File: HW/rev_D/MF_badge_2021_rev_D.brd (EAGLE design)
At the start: 61 x 100.5 mm, 167 parts, among them IC1 MCP73831, J1 HRO_31_M_12_USB_C, Q2 DMG3415U-7, Q3 DMG3415U-7, Q4 DMG3415U-7, Q5 Si2305, Q6 SI1308EDL-T1-GE3, U1 ESP32-S2-WROOM, U2 AP2112K-3.3, X1 CAPTOUCH_10MM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

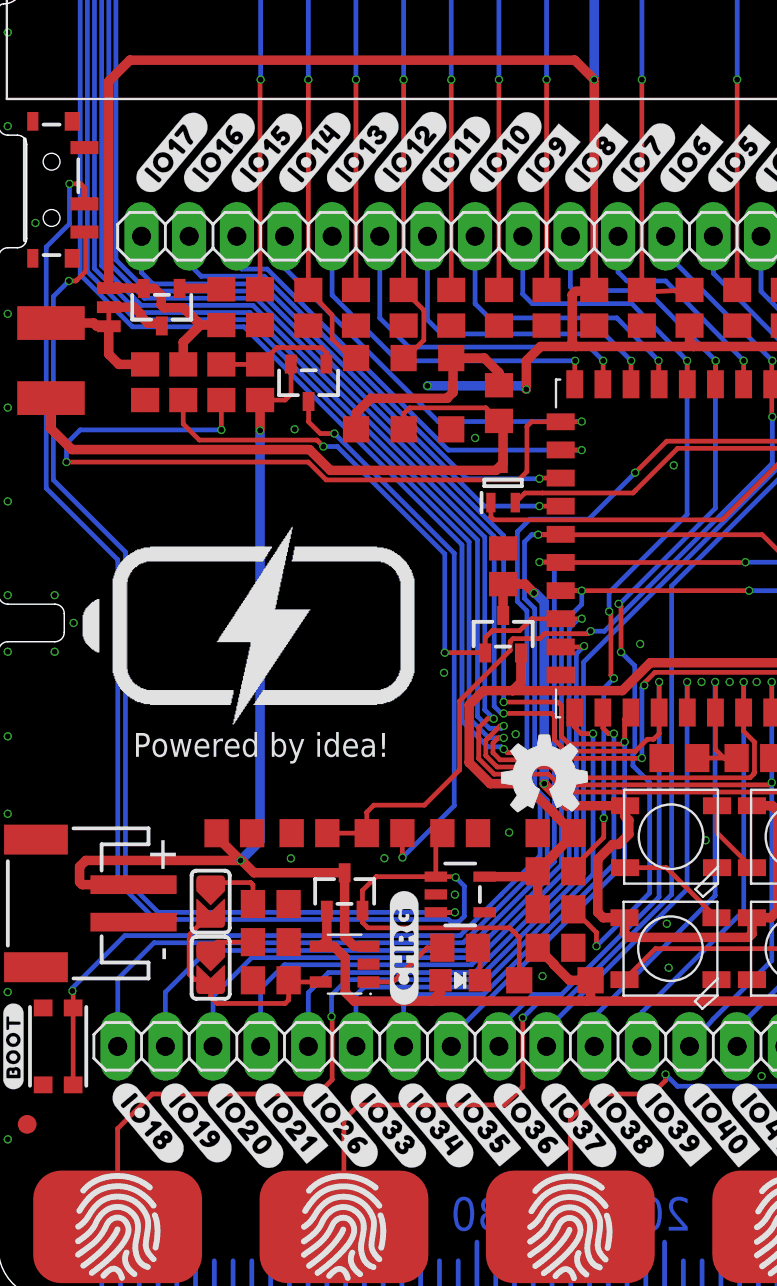
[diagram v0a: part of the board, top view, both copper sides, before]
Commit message: Update
- add pin to drive Q4
- changed pin labels to match reality
- add .gitignore file
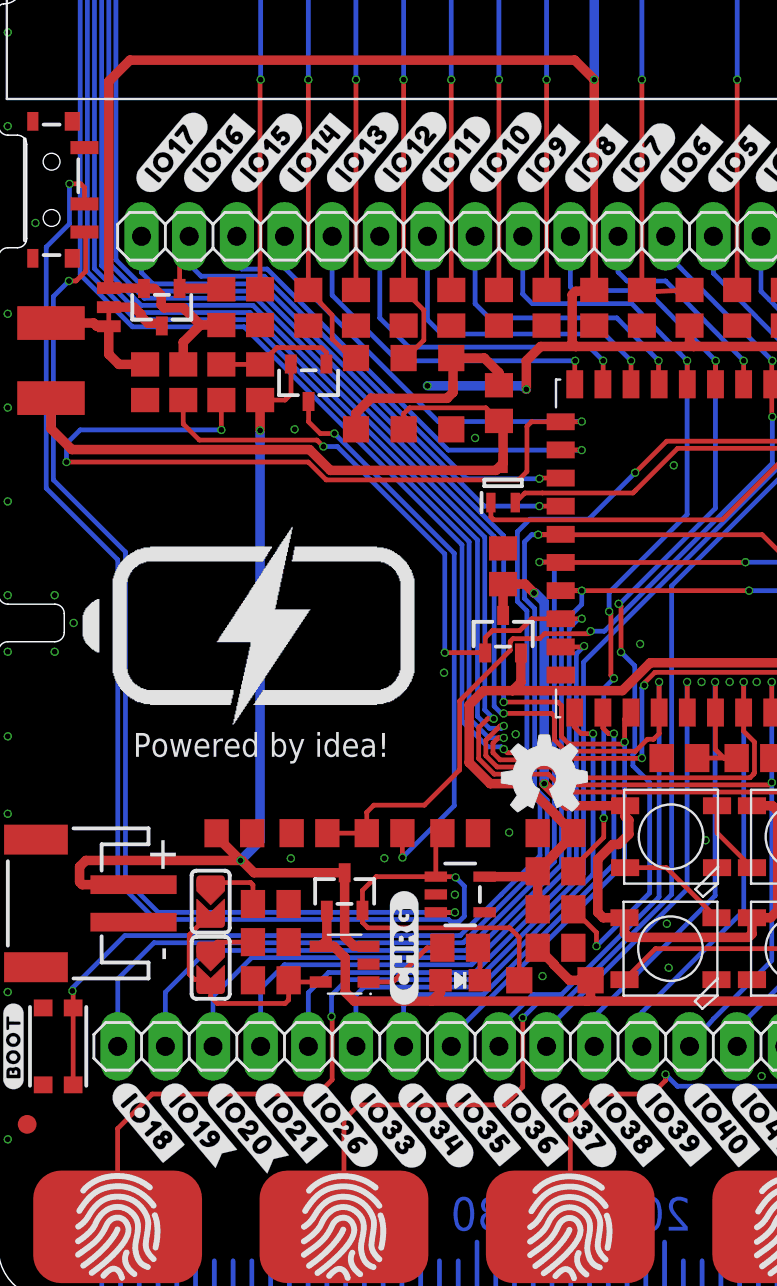
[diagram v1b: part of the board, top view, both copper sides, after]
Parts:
- C1, C11, C2, C3, C4, C5, C6: value 1u -> 1uF
- renumbered Q6 to Q1
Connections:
- removed net N$27: Q4.1, R13.1
- net IO16: now also Q4.1, R13.1
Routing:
- net IO16: track 26.0 -> 31.3 mm
- net N$27: track 2.25 -> 0.00 mm
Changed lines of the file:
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@@
 <layer number="20" name="Dimension" color="24" fill="1" visible="yes" active="yes"/>
 <layer number="21" name="tPlace" color="7" fill="1" visible="yes" active="yes"/>
-<layer number="22" name="bPlace" color="7" fill="1" visible="yes" active="yes"/>
+<layer number="22" name="bPlace" color="7" fill="1" visible="no" active="yes"/>
 <layer number="23" name="tOrigins" color="15" fill="1" visible="yes" active="yes"/>
 <layer number="24" name="bOrigins" color="15" fill="1" visible="yes" active="yes"/>
@@
 <layer number="38" name="bTest" color="7" fill="1" visible="no" active="yes"/>
 <layer number="39" name="tKeepout" color="4" fill="11" visible="yes" active="yes"/>
-<layer number="40" name="bKeepout" color="1" fill="11" visible="yes" active="yes"/>
-<layer number="41" name="tRestrict" color="4" fill="10" visible="yes" active="yes"/>
-<layer number="42" name="bRestrict" color="1" fill="10" visible="yes" active="yes"/>
+<layer number="40" name="bKeepout" color="1" fill="11" visible="no" active="yes"/>
+<layer number="41" name="tRestrict" color="4" fill="10" visible="no" active="yes"/>
+<layer number="42" name="bRestrict" color="1" fill="10" visible="no" active="yes"/>
 <layer number="43" name="vRestrict" color="2" fill="10" visible="no" active="yes"/>
 <layer number="44" name="Drills" color="7" fill="1" visible="no" active="yes"/>
@@
 </groups>
 <elements>
-<element name="C1" library="rcl" library_urn="urn:adsk.eagle:library:334" package="C0805" package3d_urn="urn:adsk.eagle:package:23617/2" value="1u" x="13.93825" y="52.83175" smashed="yes" rot="R270">
+<element name="C1" library="rcl" library_urn="urn:adsk.eagle:library:334" package="C0805" package3d_urn="urn:adsk.eagle:package:23617/2" value="1uF" x="13.93825" y="52.83175" smashed="yes" rot="R270">
 <attribute name="POPULARITY" value="88" x="-47.02175" y="-6.85825" size="1.778" layer="27" rot="R270" display="off"/>
 <attribute name="SPICEPREFIX" value="C" x="-47.02175" y="-6.85825" size="1.778" layer="27" rot="R270" display="off"/>
@@
 <attribute name="VALUE" x="25.02" y="48.52" size="1.016" layer="27" rot="R270"/>
 </element>
-<element name="C11" library="rcl" library_urn="urn:adsk.eagle:library:334" package="C0805" package3d_urn="urn:adsk.eagle:package:23617/2" value="1u" x="29.21" y="52.8" smashed="yes" rot="R270">
+<element name="C11" library="rcl" library_urn="urn:adsk.eagle:library:334" package="C0805" package3d_urn="urn:adsk.eagle:package:23617/2" value="1uF" x="29.21" y="52.8" smashed="yes" rot="R270">
 <attribute name="POPULARITY" value="88" x="-31.75" y="-3.08" size="1.778" layer="27" rot="R270" display="off"/>
 <attribute name="SPICEPREFIX" value="C" x="-31.75" y="-3.08" size="1.778" layer="27" rot="R270" display="off"/>
@@
 <attribute name="VALUE" x="47.88" y="53.6" size="1.016" layer="27" rot="R270"/>
 </element>
-<element name="C2" library="rcl" library_urn="urn:adsk.eagle:library:334" package="C0805" package3d_urn="urn:adsk.eagle:package:23617/2" value="1u" x="16.51" y="52.8" smashed="yes" rot="R270">
+<element name="C2" library="rcl" library_urn="urn:adsk.eagle:library:334" package="C0805" package3d_urn="urn:adsk.eagle:package:23617/2" value="1uF" x="16.51" y="52.8" smashed="yes" rot="R270">
 <attribute name="POPULARITY" value="88" x="-49.53" y="37.56" size="1.778" layer="27" rot="R270" display="off"/>
 <attribute name="SPICEPREFIX" value="C" x="-49.53" y="37.56" size="1.778" layer="27" rot="R270" display="off"/>
 <attribute name="VALUE" x="14.86" y="53.6" size="1.016" layer="27" rot="R270"/>
 </element>
-<element name="C3" library="rcl" library_urn="urn:adsk.eagle:library:334" package="C0805" package3d_urn="urn:adsk.eagle:package:23617/2" value="1u" x="19.05" y="52.8" smashed="yes" rot="R270">
+<element name="C3" library="rcl" library_urn="urn:adsk.eagle:library:334" package="C0805" package3d_urn="urn:adsk.eagle:package:23617/2" value="1uF" x="19.05" y="52.8" smashed="yes" rot="R270">
 <attribute name="POPULARITY" value="88" x="-46.99" y="33.75" size="1.778" layer="27" rot="R270" display="off"/>
 <attribute name="SPICEPREFIX" value="C" x="-46.99" y="33.75" size="1.778" layer="27" rot="R270" display="off"/>
 <attribute name="VALUE" x="17.4" y="53.6" size="1.016" layer="27" rot="R270"/>
 </element>
-<element name="C4" library="rcl" library_urn="urn:adsk.eagle:library:334" package="C0805" package3d_urn="urn:adsk.eagle:package:23617/2" value="1u" x="21.59" y="52.8" smashed="yes" rot="R270">
+<element name="C4" library="rcl" library_urn="urn:adsk.eagle:library:334" package="C0805" package3d_urn="urn:adsk.eagle:package:23617/2" value="1uF" x="21.59" y="52.8" smashed="yes" rot="R270">
 <attribute name="POPULARITY" value="88" x="-44.45" y="29.94" size="1.778" layer="27" rot="R270" display="off"/>
 <attribute name="SPICEPREFIX" value="C" x="-44.45" y="29.94" size="1.778" layer="27" rot="R270" display="off"/>
 <attribute name="VALUE" x="19.94" y="53.6" size="1.016" layer="27" rot="R270"/>
 </element>
-<element name="C5" library="rcl" library_urn="urn:adsk.eagle:library:334" package="C0805" package3d_urn="urn:adsk.eagle:package:23617/2" value="1u" x="24.13" y="52.8" smashed="yes" rot="R270">
+<element name="C5" library="rcl" library_urn="urn:adsk.eagle:library:334" package="C0805" package3d_urn="urn:adsk.eagle:package:23617/2" value="1uF" x="24.13" y="52.8" smashed="yes" rot="R270">
 <attribute name="POPULARITY" value="88" x="-41.91" y="26.13" size="1.778" layer="27" rot="R270" display="off"/>
 <attribute name="SPICEPREFIX" value="C" x="-41.91" y="26.13" size="1.778" layer="27" rot="R270" display="off"/>
 <attribute name="VALUE" x="22.48" y="53.6" size="1.016" layer="27" rot="R270"/>
 </element>
-<element name="C6" library="rcl" library_urn="urn:adsk.eagle:library:334" package="C0805" package3d_urn="urn:adsk.eagle:package:23617/2" value="1u" x="26.67" y="52.8" smashed="yes" rot="R270">
+<element name="C6" library="rcl" library_urn="urn:adsk.eagle:library:334" package="C0805" package3d_urn="urn:adsk.eagle:package:23617/2" value="1uF" x="26.67" y="52.8" smashed="yes" rot="R270">
 <attribute name="POPULARITY" value="88" x="-39.37" y="22.32" size="1.778" layer="27" rot="R270" display="off"/>
 <attribute name="SPICEPREFIX" value="C" x="-39.37" y="22.32" size="1.778" layer="27" rot="R270" display="off"/>
@@
 <attribute name="VALUE" x="9.3345" y="50.1015" size="1.27" layer="27" rot="R270"/>
 </element>
-<element name="Q6" library="SamacSys_Parts" package="SOT65P210X110-3N" value="SI1308EDL-T1-GE3" x="26.89225" y="43.46575" smashed="yes" rot="R90">
+<element name="Q1" library="SamacSys_Parts" package="SOT65P210X110-3N" value="SI1308EDL-T1-GE3" x="26.89225" y="43.46575" smashed="yes" rot="R90">
 <attribute name="DESCRIPTION" value="MOSFET N-Ch 30V 1.5A TrenchFET SC70 Vishay Si1308EDL-T1-GE3 N-channel MOSFET Transistor, 1.5 A, 30 V, 3-Pin SC-70" x="26.89225" y="43.46575" size="1.778" layer="27" rot="R90" display="off"/>
 <attribute name="HEIGHT" value="1.1mm" x="26.89225" y="43.46575" size="1.778" layer="27" rot="R90" display="off"/>
@@
 <wire x1="41.17" y1="83.48" x2="44.45" y2="80.2" width="0.254" layer="16"/>
 <wire x1="44.45" y1="53.75" x2="44.45" y2="64.96" width="0.254" layer="1"/>
-<contactref element="Q6" pad="2"/>
+<contactref element="Q1" pad="2"/>
 <wire x1="27.54225" y1="42.41575" x2="28.0535" y2="42.927" width="0.254" layer="1"/>
 <wire x1="28.0535" y1="42.927" x2="28.98775" y2="42.927" width="0.254" layer="1"/>
@@
 <wire x1="44.48" y1="83.98" x2="46.99" y2="81.47" width="0.254" layer="16"/>
 <wire x1="46.99" y1="53.75" x2="46.99" y2="64.96" width="0.254" layer="1"/>
-<contactref element="Q6" pad="1"/>
+<contactref element="Q1" pad="1"/>
 <wire x1="26.24225" y1="42.41575" x2="26.24225" y2="41.63925" width="0.254" layer="1"/>
 <wire x1="26.24225" y1="41.63925" x2="26.3845" y2="41.497" width="0.254" layer="1"/>
@@
 <wire x1="29.962" y1="43.723" x2="28.86425" y2="43.723" width="0.254" layer="1"/>
 <wire x1="28.86425" y1="43.723" x2="28.829" y2="43.68775" width="0.254" layer="1"/>
+<contactref element="Q4" pad="1"/>
+<contactref element="R13" pad="1"/>
+<wire x1="9.6495" y1="53.83175" x2="11.8245" y2="53.83175" width="0.508" layer="1"/>
+<wire x1="11.8245" y1="53.83175" x2="11.8745" y2="53.78175" width="0.508" layer="1"/>
+<wire x1="9.6495" y1="53.83175" x2="9.6495" y2="56.0995" width="0.254" layer="1"/>
+<wire x1="9.6495" y1="56.0995" x2="10.16" y2="56.61" width="0.254" layer="1"/>
 </signal>
 <signal name="IO17">
@@
 <contactref element="D1" pad="A"/>
 <contactref element="L1" pad="2"/>
-<contactref element="Q6" pad="3"/>
+<contactref element="Q1" pad="3"/>
 <wire x1="26.89225" y1="46.54775" x2="26.89225" y2="44.51575" width="0.508" layer="1"/>
 <wire x1="26.509" y1="44.1325" x2="26.89225" y2="44.51575" width="0.508" layer="1"/>
@@
 <wire x1="5.87375" y1="51.81575" x2="5.68325" y2="51.81575" width="0" layer="19" extent="1-1"/>
 </signal>
-<signal name="N$27">
-<contactref element="Q4" pad="1"/>
-<contactref element="R13" pad="1"/>
-<wire x1="9.6495" y1="53.83175" x2="11.8245" y2="53.83175" width="0.508" layer="1"/>
-<wire x1="11.8245" y1="53.83175" x2="11.8745" y2="53.78175" width="0.508" layer="1"/>
-</signal>
 <signal name="N$78">

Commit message: Verified design files for rev.D
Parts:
- removed JP1: JUMPER-SMT_3_1-NC_TRACE_NO-SILK, SparkFun-Jumpers:SMT-JUMPER_3_1-NC_TRACE_NO-SILK
- moved L1 1.97 mm to (4.76, 49.8)
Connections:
- removed net N$78: JP1.2, Q4.3
- net +3V3: no longer JP1.1
- net N$26: now also Q4.3; no longer JP1.3
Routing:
- net +3V3: track 204.8 -> 194.6 mm, vias 3 -> 1
- net N$78: track 3.30 -> 0.00 mm
- net N$19: track 35.5 -> 33.7 mm
- net N$26: track 6.70 -> 7.40 mm
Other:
- board text added: "Maker badge"
- board text removed: "Maker Badge"
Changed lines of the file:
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@@
 <rectangle x1="54.32625" y1="6.67875" x2="54.83025" y2="6.68575" layer="21"/>
 <rectangle x1="54.43825" y1="6.68575" x2="54.71125" y2="6.69275" layer="21"/>
-<text x="30.5435" y="97.2815" size="3.5" layer="21" font="vector" ratio="15" align="center">Maker Badge</text>
+<text x="30.5435" y="97.2815" size="3.5" layer="21" font="vector" ratio="15" align="center">Maker badge</text>
 <wire x1="45.5" y1="3" x2="45.5" y2="0" width="0.254" layer="30"/>
 <wire x1="46.5" y1="2" x2="46.5" y2="0" width="0.254" layer="30"/>
@@
 </element>
 <element name="J1" library="esp32-s2_ePaper" package="HRO_31_M_12_USB_C" package3d_urn="urn:adsk.eagle:package:12796916/9" value="HRO_31_M_12_USB_C" x="57.531" y="23.082" smashed="yes" rot="R90"/>
-<element name="L1" library="rcl" library_urn="urn:adsk.eagle:library:334" package="L4532P" package3d_urn="urn:adsk.eagle:package:23484/1" value="68uH" x="2.794" y="49.98625" smashed="yes" rot="R270">
-<attribute name="POPULARITY" value="0" x="-2.286" y="-8.43375" size="1.778" layer="27" rot="R270" display="off"/>
-<attribute name="SPICEPREFIX" value="L" x="-2.286" y="-8.43375" size="1.778" layer="27" rot="R270" display="off"/>
-<attribute name="VALUE" x="-1.016" y="51.89125" size="1.27" layer="27" rot="R270"/>
+<element name="L1" library="rcl" library_urn="urn:adsk.eagle:library:334" package="L4532P" package3d_urn="urn:adsk.eagle:package:23484/1" value="68uH" x="4.7625" y="49.8275" smashed="yes" rot="R270">
+<attribute name="POPULARITY" value="0" x="-0.3175" y="-8.5925" size="1.778" layer="27" rot="R270" display="off"/>
+<attribute name="SPICEPREFIX" value="L" x="-0.3175" y="-8.5925" size="1.778" layer="27" rot="R270" display="off"/>
+<attribute name="VALUE" x="0.9525" y="51.7325" size="1.27" layer="27" rot="R270"/>
 </element>
 <element name="R1" library="rcl" library_urn="urn:adsk.eagle:library:334" package="R0805" package3d_urn="urn:adsk.eagle:package:23553/2" value="10K" x="46.99" y="52.8" smashed="yes" rot="R270">
@@
 <attribute name="VALUE" x="9.3345" y="53.46675" size="1.27" layer="27" rot="R270"/>
 </element>
-<element name="JP1" library="SparkFun-Jumpers" package="SMT-JUMPER_3_1-NC_TRACE_NO-SILK" value="JUMPER-SMT_3_1-NC_TRACE_NO-SILK" x="5.87375" y="52.83175" smashed="yes" rot="R270">
-<attribute name="VALUE" x="4.73075" y="52.83175" size="0.6096" layer="27" font="vector" ratio="20" rot="R270" align="top-center"/>
-</element>
 <element name="Q5" library="microbuilder" package="SOT23-R" value="Si2305" x="16.523" y="48.80425" smashed="yes" rot="R180">
 <attribute name="VALUE" x="14.745" y="49.43925" size="0.4064" layer="27" ratio="10" rot="R180"/>
@@
 <contactref element="Q4" pad="2"/>
 <contactref element="R13" pad="2"/>
-<contactref element="JP1" pad="1"/>
-<via x="22.86" y="48.641" extent="1-16" drill="0.3"/>
-<wire x1="22.86" y1="48.641" x2="27.94" y2="48.641" width="0.508" layer="16"/>
-<wire x1="27.94" y1="48.641" x2="28.1305" y2="48.4505" width="0.508" layer="16"/>
-<via x="28.1305" y="48.4505" extent="1-16" drill="0.3"/>
-<wire x1="28.1305" y1="48.4505" x2="28.1305" y2="49.9745" width="0.508" layer="1"/>
-<wire x1="28.89225" y1="50.73625" x2="30.76575" y2="50.73625" width="0.508" layer="1"/>
-<wire x1="28.1305" y1="49.9745" x2="28.89225" y2="50.73625" width="0.508" layer="1"/>
 <wire x1="11.8745" y1="51.88175" x2="10.761" y2="51.88175" width="0.508" layer="1"/>
 <wire x1="9.8425" y1="52.80025" x2="8.8265" y2="52.80025" width="0.508" layer="1"/>
@@
 <wire x1="8.303" y1="53.83175" x2="7.7495" y2="53.83175" width="0.508" layer="1"/>
 <wire x1="10.761" y1="51.88175" x2="9.8425" y2="52.80025" width="0.508" layer="1"/>
-<wire x1="5.87375" y1="53.84775" x2="7.7335" y2="53.84775" width="0.508" layer="1"/>
 <wire x1="7.7335" y1="53.84775" x2="7.7495" y2="53.83175" width="0.508" layer="1"/>
 <wire x1="25.9061" y1="22.47625" x2="28.44775" y2="22.47625" width="0.508" layer="1"/>
@@
 <wire x1="9.8435" y1="50.96425" x2="10.761" y2="51.88175" width="0.508" layer="1"/>
 <wire x1="31.75" y1="60.29325" x2="31.75" y2="64.96" width="0.508" layer="1"/>
-<wire x1="5.87375" y1="64.87375" x2="7" y2="66" width="0.508" layer="1"/>
+<wire x1="7" y1="66" x2="5.87375" y2="64.87375" width="0.508" layer="1"/>
 <wire x1="30.71" y1="66" x2="31.75" y2="64.96" width="0.508" layer="1"/>
-<wire x1="5.87375" y1="53.84775" x2="5.87375" y2="64.87375" width="0.508" layer="1"/>
 <wire x1="7" y1="66" x2="30.71" y2="66" width="0.508" layer="1"/>
 <wire x1="28.736" y1="22.7645" x2="29.605" y2="23.6335" width="0.508" layer="1"/>
@@
 <wire x1="28.067" y1="27.4053125" x2="28.067" y2="27.432" width="0.508" layer="1"/>
 <wire x1="29.7675" y1="25.7048125" x2="28.067" y2="27.4053125" width="0.508" layer="1"/>
+<wire x1="5.87375" y1="64.87375" x2="5.87375" y2="54.62625" width="0.508" layer="1"/>
+<wire x1="6.65225" y1="53.84775" x2="7.7335" y2="53.84775" width="0.508" layer="1"/>
+<wire x1="5.87375" y1="54.62625" x2="6.65225" y2="53.84775" width="0.508" layer="1"/>
 </signal>
 <signal name="GND">
@@
 <via x="0.489" y="47.479" extent="1-16" drill="0.3"/>
 <via x="0.489" y="52.479" extent="1-16" drill="0.3"/>
-<via x="1.96525" y="57.32025" extent="1-16" drill="0.3"/>
-<via x="0.489" y="62.479" extent="1-16" drill="0.3"/>
+<via x="2.09225" y="56.43125" extent="1-16" drill="0.3"/>
+<via x="0.77475" y="62.7965" extent="1-16" drill="0.3"/>
 <via x="0.489" y="67.479" extent="1-16" drill="0.3"/>
 <via x="1.743" y="72.479" extent="1-16" drill="0.3"/>
@@
 <wire x1="26.89225" y1="46.54775" x2="26.89225" y2="44.51575" width="0.508" layer="1"/>
 <wire x1="26.509" y1="44.1325" x2="26.89225" y2="44.51575" width="0.508" layer="1"/>
-<wire x1="2.794" y1="47.98625" x2="2.794" y2="46.355" width="0.508" layer="1"/>
-<wire x1="2.794" y1="46.355" x2="3.90805" y2="45.24095" width="0.508" layer="1"/>
-<wire x1="3.90805" y1="45.24095" x2="16.5763" y2="45.24095" width="0.508" layer="1"/>
+<wire x1="4.7625" y1="47.8275" x2="4.7625" y2="45.81525" width="0.508" layer="1"/>
+<wire x1="4.7625" y1="45.81525" x2="5.3368" y2="45.24095" width="0.508" layer="1"/>
+<wire x1="5.3368" y1="45.24095" x2="16.5763" y2="45.24095" width="0.508" layer="1"/>
 <wire x1="16.5763" y1="45.24095" x2="17.68475" y2="44.1325" width="0.508" layer="1"/>
 <wire x1="17.68475" y1="44.1325" x2="26.509" y2="44.1325" width="0.508" layer="1"/>
@@
 <contactref element="L1" pad="1"/>
 <contactref element="C12" pad="1"/>
-<contactref element="JP1" pad="3"/>
-<wire x1="5.87375" y1="51.81575" x2="5.93725" y2="51.75225" width="0.508" layer="1"/>
-<wire x1="2.794" y1="51.98625" x2="5.0685" y2="51.98625" width="0.508" layer="1"/>
-<wire x1="5.239" y1="51.81575" x2="5.68325" y2="51.81575" width="0.508" layer="1"/>
-<wire x1="5.0685" y1="51.98625" x2="5.239" y2="51.81575" width="0.508" layer="1"/>
-<wire x1="6.416" y1="49.7815" x2="7.81025" y2="49.7815" width="0.508" layer="1"/>
-<wire x1="5.87375" y1="51.81575" x2="5.87375" y2="50.32375" width="0.508" layer="1"/>
-<wire x1="5.87375" y1="50.32375" x2="6.416" y2="49.7815" width="0.508" layer="1"/>
-<wire x1="5.87375" y1="51.81575" x2="5.68325" y2="51.81575" width="0" layer="19" extent="1-1"/>
-</signal>
-<signal name="N$78">
-<contactref element="JP1" pad="2"/>
 <contactref element="Q4" pad="3"/>
-<wire x1="8.6995" y1="51.83175" x2="8.5565" y2="51.97475" width="0.508" layer="1"/>
-<wire x1="8.5565" y1="51.97475" x2="7.96925" y2="51.97475" width="0.508" layer="1"/>
-<wire x1="7.96925" y1="51.97475" x2="7.58825" y2="52.35575" width="0.508" layer="1"/>
-<wire x1="7.58825" y1="52.35575" x2="7.58825" y2="52.451" width="0.508" layer="1"/>
-<wire x1="7.2075" y1="52.83175" x2="7.58825" y2="52.451" width="0.508" layer="1"/>
-<wire x1="5.87375" y1="52.83175" x2="7.2075" y2="52.83175" width="0.508" layer="1"/>
+<wire x1="7.81025" y1="49.7815" x2="5.7185" y2="49.7815" width="0.508" layer="1"/>
+<wire x1="5.7185" y1="49.7815" x2="4.2175" y2="51.2825" width="0.508" layer="1"/>
+<wire x1="4.2175" y1="51.2825" x2="4.7625" y2="51.8275" width="0.508" layer="1"/>
+<wire x1="8.6995" y1="51.83175" x2="8.6995" y2="50.67075" width="0.508" layer="1"/>
+<wire x1="8.6995" y1="50.67075" x2="7.81025" y2="49.7815" width="0.508" layer="1"/>
 </signal>
 <signal name="N$79">

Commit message: Add ESPRESSIF logo
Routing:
- net IO41_CS: track 111.4 -> 104.1 mm, vias 2 -> 3
- net IO39_RST: track 110.8 -> 104.6 mm, vias 2 -> 3
- net IO9_SCL: track 44.5 -> 50.6 mm
- net IO40_DC: track 107.8 -> 104.5 mm
- net IO38: track 28.4 -> 25.9 mm, vias 1 -> 2
- net +3V3: track 194.6 -> 192.5 mm
- net IO35_MOSI: track 92.7 -> 90.6 mm
- net IO36_SCK: track 100.9 -> 98.9 mm
- net IO42_BUSY: track 114.0 -> 115.9 mm
- net IO8_SDA: track 51.2 -> 50.0 mm
- net IO34: track 25.0 -> 24.4 mm
- net V+: track 53.1 -> 53.6 mm, vias 2 -> 4
- net GND: vias 73 -> 71
